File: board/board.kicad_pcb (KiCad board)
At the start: 2 copper layers, 21 x 13 mm, 14 parts, among them J1 001_I2C, J2 001_I2C, U1 MCP9844x-xMN

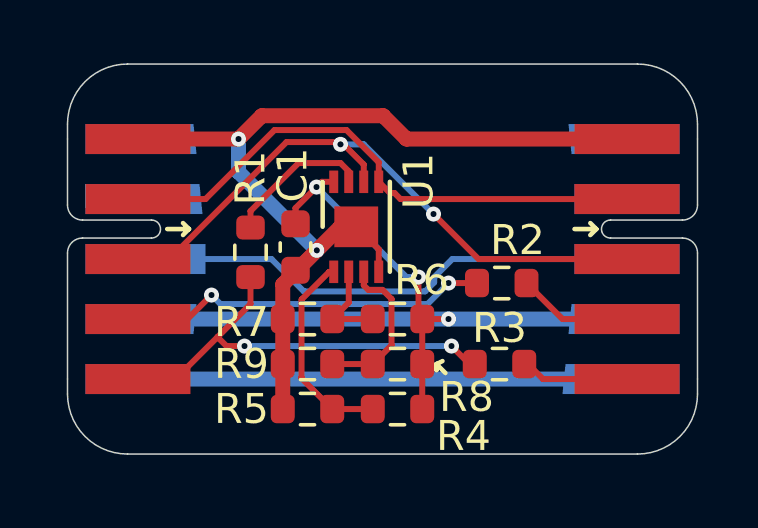
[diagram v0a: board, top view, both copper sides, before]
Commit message: added board name on silkscreen
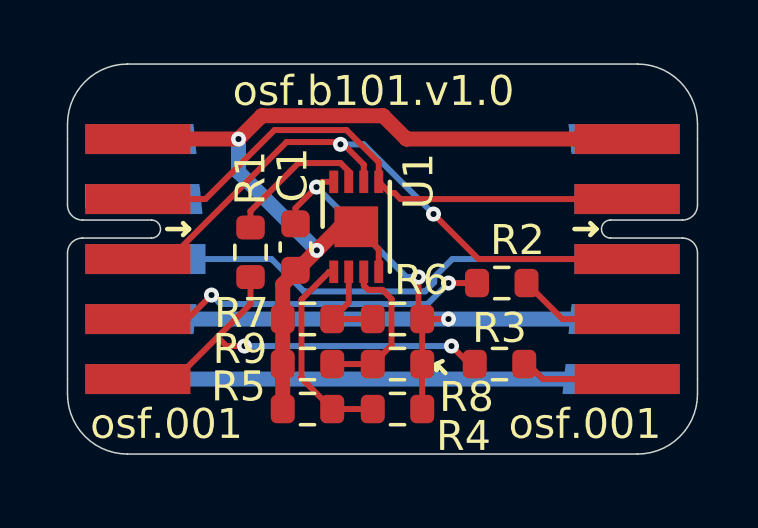
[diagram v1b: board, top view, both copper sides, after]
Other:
- board text added: "osf.001"
- board text added: "osf.b101.v1.0"
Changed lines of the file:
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@@
     (property "Sheetname" "temperature")
     (attr smd)
-    (fp_text reference "R9" (at -2.2 0) (layer "F.SilkS")
+    (fp_text reference "R9" (at -2.25 -0.5) (layer "F.SilkS")
       (effects (font (size 1 1) (thickness 0.15)))
     )
@@
     (property "Sheetname" "temperature")
     (attr smd)
-    (fp_text reference "R7" (at -2.2 0.1) (layer "F.SilkS")
+    (fp_text reference "R7" (at -2.2 -0.2) (layer "F.SilkS")
       (effects (font (size 1 1) (thickness 0.15)))
     )
@@
     (property "Sheetname" "temperature")
     (attr smd)
-    (fp_text reference "R5" (at -2.2 0) (layer "F.SilkS")
+    (fp_text reference "R5" (at -2.3 -0.75) (layer "F.SilkS")
       (effects (font (size 1 1) (thickness 0.15)))
     )
@@
   (gr_line (start 140 92.5) (end 140 92) (layer "Edge.Cuts") (width 0.05))
   (gr_arc (start 140 92) (mid 140.585786 90.585786) (end 142 90) (layer "Edge.Cuts") (width 0.05))
+  (gr_text "osf.b101.v1.0" (at 150.2 90.9) (layer "F.SilkS")
+    (effects (font (size 1 1) (thickness 0.15)))
+  )
+  (gr_text "osf.001" (at 143.3 102) (layer "F.SilkS")
+    (effects (font (size 1 1) (thickness 0.15)))
+  )
+  (gr_text "osf.001" (at 157.25 102) (layer "F.SilkS")
+    (effects (font (size 1 1) (thickness 0.15)))
+  )
   (segment (start 149.375 93.575) (end 149.1 93.3) (width 0.2) (layer "F.Cu") (net 1))
   (segment (start 149.1 93.3) (end 147.7 93.3) (width 0.2) (layer "F.Cu") (net 1))
